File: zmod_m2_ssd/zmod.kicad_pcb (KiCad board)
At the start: 6 copper layers, 50 x 70 mm, 16 parts, among them J1 MDT420M02001, J2 QTH-020-01-X-D-DP-A, U1 SN74LVC1T45DBV

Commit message: adding clock chips for M.2
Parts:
- added U2: LTC6957xMS-2, Package_SO:MSOP-12_3x4mm_P0.65mm, F.Cu at (112.0, 89.0)
- added X1: ECS-2520MV-xxx-xx, Oscillator:Oscillator_SMD_ECS_2520MV-xxx-xx-4Pin_2.5x2.0mm, F.Cu at (105.0, 90.0)

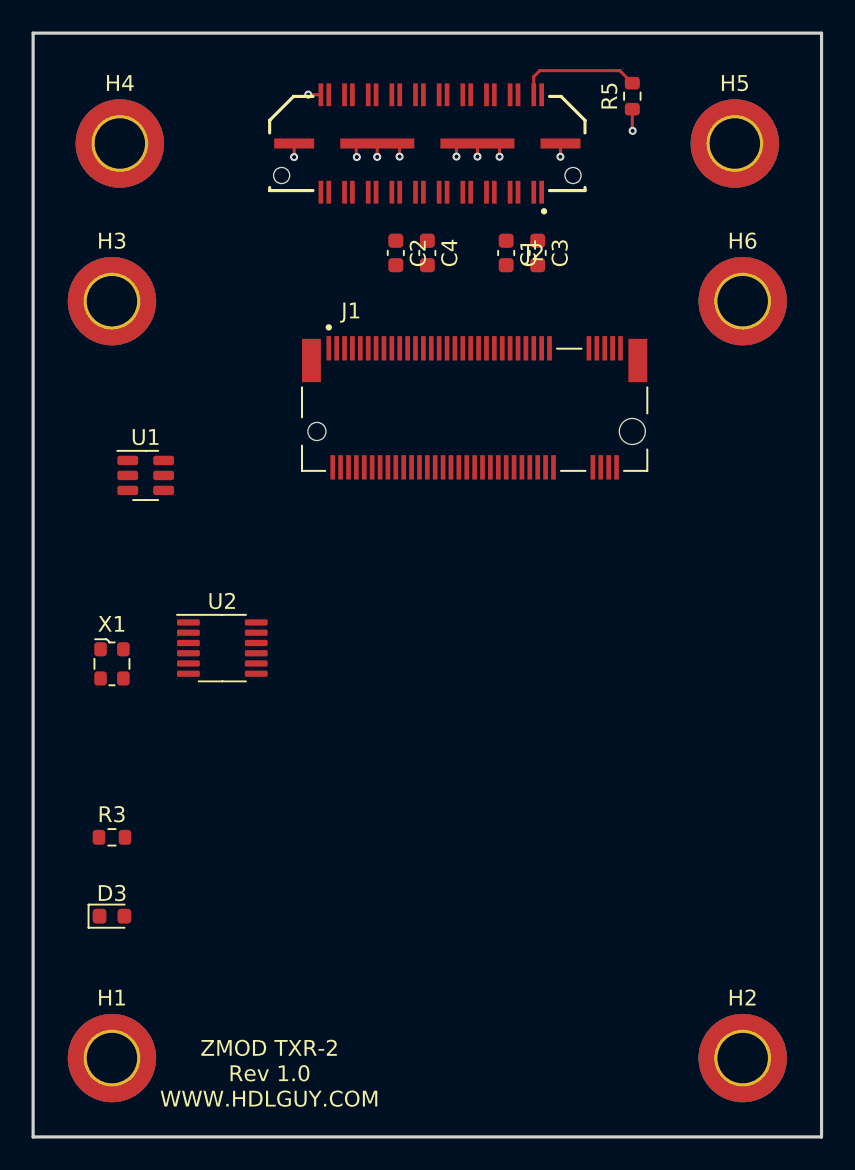
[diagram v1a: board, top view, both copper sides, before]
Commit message: placed all components and locked down mounting holes and connectors, need M.2 screw hole
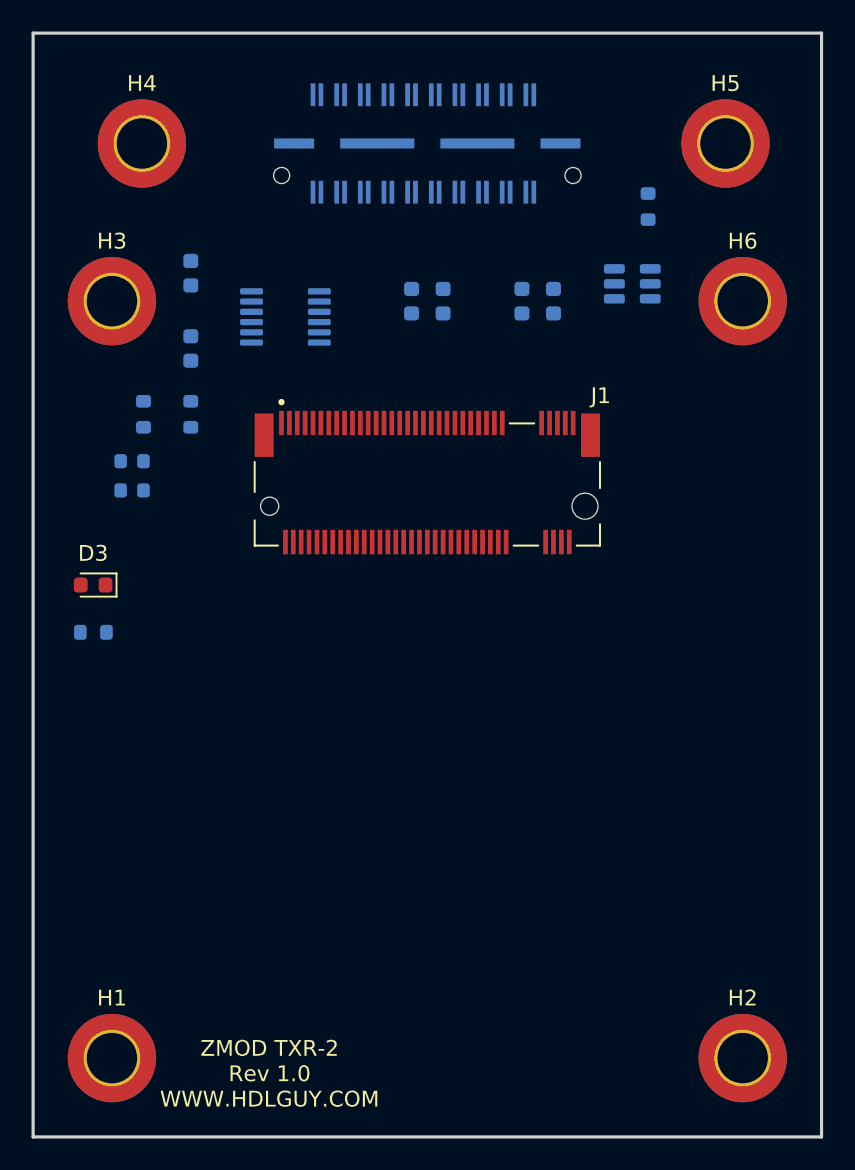
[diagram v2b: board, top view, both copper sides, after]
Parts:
- added C5: 0.01uf, Capacitor_SMD:C_0603_1608Metric, B.Cu at (110.0, 65.2)
- added C6: 0.01uf, Capacitor_SMD:C_0603_1608Metric, B.Cu at (110.0, 70.0)
- added R1: 100, Resistor_SMD:R_0603_1608Metric, B.Cu at (107.0, 74.2)
- added R2: 49.9, Resistor_SMD:R_0603_1608Metric, B.Cu at (110.0, 74.2)
- C1, C2, C3, C4: value C -> 0.01uf; moved to B.Cu
- J2, R3, R5, U1, U2: moved to B.Cu
- X1: value ECS-2520MV-xxx-xx -> ECS-2520MVQ-1000-BN-TR; moved to B.Cu
- moved U1 33.2 mm to (138.0, 65.9), turned to 180 degrees
- moved U2 21.4 mm to (116.0, 68.0)
- moved D3 21.0 mm to (103.8, 85.0), turned to 180 degrees
- moved R3 13.1 mm to (103.8, 88.0), turned to 180 degrees
- moved X1 12.0 mm to (106.3, 78.1)
- moved R5 7.07 mm to (139.0, 61.0)
- moved J1 5.61 mm to (125.0, 80.0)
- moved C1 3.22 mm to (131.0, 67.0)
- moved C2 3.22 mm to (124.0, 67.0)
- moved C3 3.22 mm to (133.0, 67.0)
- moved C4 3.22 mm to (126.0, 67.0)
- moved H4 1.40 mm to (106.9, 57.0)
- moved H5 0.59 mm to (143.9, 57.0)
- turned J2 to 0 degrees
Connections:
- net Net-(C1-Pad2) renamed /gtr0_txn_cc
- net Net-(C2-Pad2) renamed /gtr1_txn_cc
- net Net-(C3-Pad2) renamed /gtr0_txp_cc
- net Net-(C4-Pad2) renamed /gtr1_txp_cc
- J1 pad 53: unconnected-(J1-Pad53) -> Net-(U2-Pad11)
- J1 pad 55: unconnected-(J1-Pad55) -> Net-(U2-Pad10)
- U2 pad 1: unconnected-(U2-Pad1) -> GND
- U2 pad 10: unconnected-(U2-Pad10) -> Net-(U2-Pad10)
- U2 pad 11: unconnected-(U2-Pad11) -> Net-(U2-Pad11)
- U2 pad 12: unconnected-(U2-Pad12) -> GND
- U2 pad 2: unconnected-(U2-Pad2) -> +3V3
- U2 pad 3: unconnected-(U2-Pad3) -> Net-(C6-Pad2)
- U2 pad 4: unconnected-(U2-Pad4) -> Net-(C5-Pad2)
- U2 pad 5: unconnected-(U2-Pad5) -> GND
- U2 pad 6: unconnected-(U2-Pad6) -> +3V3
- U2 pad 7: unconnected-(U2-Pad7) -> GND
- U2 pad 8: unconnected-(U2-Pad8) -> /gtrclk0_p
- U2 pad 9: unconnected-(U2-Pad9) -> /gtrclk0_n
- X1 pad 2: unconnected-(X1-Pad2) -> GND
- X1 pad 3: unconnected-(X1-Pad3) -> Net-(R1-Pad2)
- X1 pad 4: unconnected-(X1-Pad4) -> +3V3
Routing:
- net /R_GA: track 7.89 -> 0.00 mm
- net GND: track 6.59 -> 0.00 mm, vias 8 -> 0
- net +3V3: track 2.19 -> 0.00 mm, vias 2 -> 0

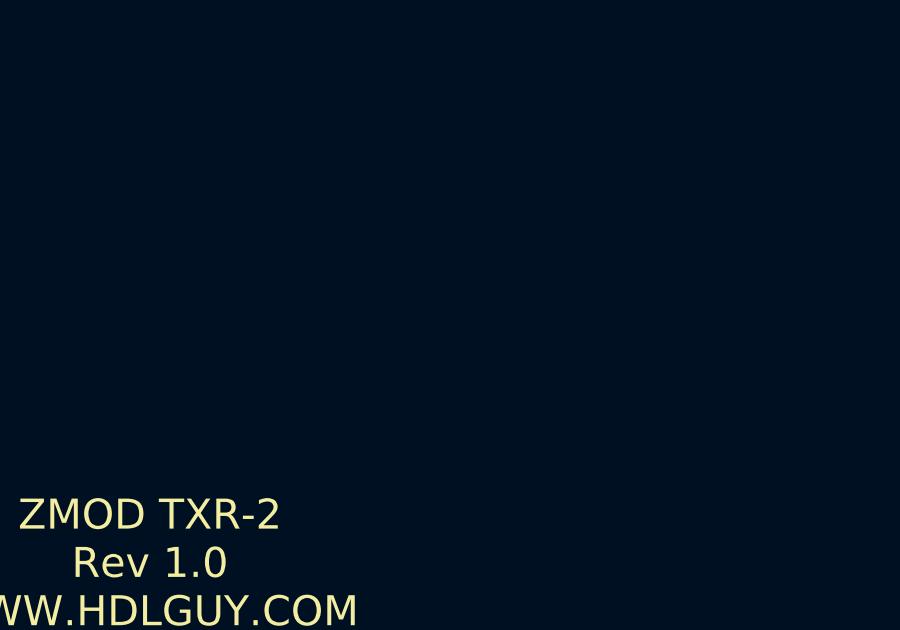
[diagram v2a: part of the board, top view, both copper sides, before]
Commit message: added mounting hole for M.2 screw
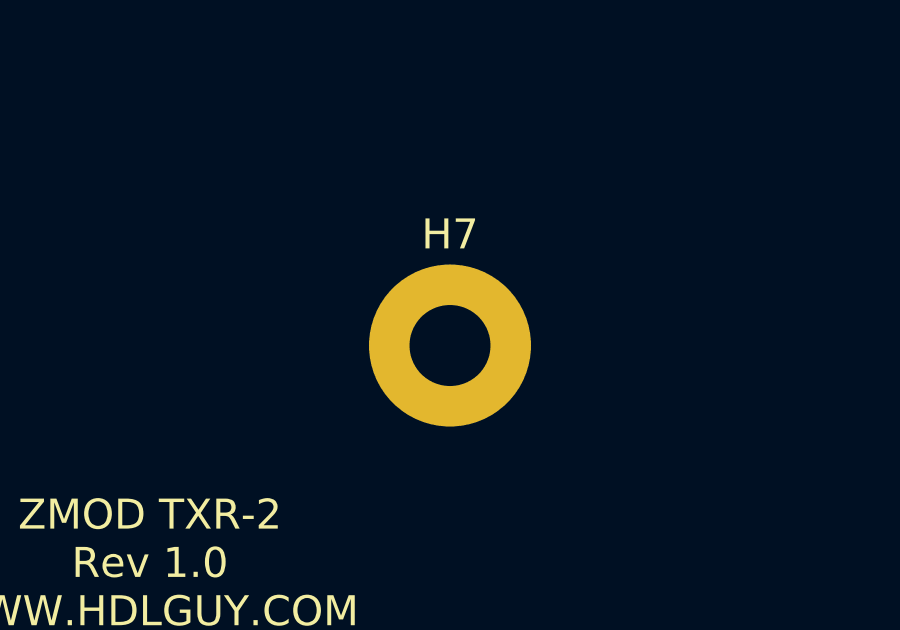
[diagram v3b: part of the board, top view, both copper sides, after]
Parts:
- added H7: MountingHole_Pad, MountingHole:MountingHole_2.7mm_Pad, F.Cu at (125.0, 108.8)
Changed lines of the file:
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@@
   (net 77 "+1V8")
   (net 78 "Net-(C6-Pad2)")
-  (net 79 "Net-(U2-Pad11)")
-  (net 80 "Net-(U2-Pad10)")
+  (net 79 "unconnected-(H7-Pad1)")
+  (net 80 "Net-(J1-Pad53)")
   (net 81 "Net-(R1-Pad2)")
   (net 82 "unconnected-(X1-Pad1)")
+  (net 83 "Net-(J1-Pad55)")
+  (footprint "MountingHole:MountingHole_2.7mm_Pad" locked (layer "F.Cu")
+    (at 125 108.75)
+    (descr "Mounting Hole 2.7mm")
+    (tags "mounting hole 2.7mm")
+    (property "Sheetfile" "zmod.kicad_sch")
+    (property "Sheetname" "")
+    (attr exclude_from_pos_files)
+    (fp_text reference "H7" (at 0 -3.7) (layer "F.SilkS")
+      (effects (font (size 1 1) (thickness 0.15)))
+    )
+    (fp_text value "MountingHole_Pad" (at 0 3.7) (layer "F.Fab")
+      (effects (font (size 1 1) (thickness 0.15)))
+    )
+    (fp_text user "${REFERENCE}" (at 0 0) (layer "F.Fab")
+      (effects (font (size 1 1) (thickness 0.15)))
+    )
+    (fp_circle (center 0 0) (end 2.7 0) (layer "Cmts.User") (width 0.15) (fill none))
+    (fp_circle (center 0 0) (end 2.95 0) (layer "F.CrtYd") (width 0.05) (fill none))
+    (pad "1" thru_hole circle locked (at 0 0) (size 5.4 5.4) (drill 2.7) (layers *.Cu *.Mask)
+      (net 79 "unconnected-(H7-Pad1)") (pinfunction "1") (pintype "input"))
+  )
   (footprint "MountingHole:MountingHole_3.2mm_M3_DIN965_Pad_TopBottom" locked (layer "F.Cu")
     (at 145 67)
@@
       (net 66 "unconnected-(J1-Pad52)") (pinfunction "~{CLKREQ}") (pintype "bidirectional+no_connect"))
     (pad "53" smd rect locked (at 3.75 -5.275) (size 0.3 1.55) (layers "F.Cu" "F.Paste" "F.Mask")
-      (net 79 "Net-(U2-Pad11)") (pinfunction "REFCLKn") (pintype "output"))
+      (net 80 "Net-(J1-Pad53)") (pinfunction "REFCLKn") (pintype "output"))
     (pad "54" smd rect locked (at 4 2.275) (size 0.3 1.55) (layers "F.Cu" "F.Paste" "F.Mask")
       (net 67 "unconnected-(J1-Pad54)") (pinfunction "~{PEWAKE}") (pintype "bidirectional+no_connect"))
     (pad "55" smd rect locked (at 4.25 -5.275) (size 0.3 1.55) (layers "F.Cu" "F.Paste" "F.Mask")
-      (net 80 "Net-(U2-Pad10)") (pinfunction "REFCLKp") (pintype "output"))
+      (net 83 "Net-(J1-Pad55)") (pinfunction "REFCLKp") (pintype "output"))
     (pad "56" smd rect locked (at 4.5 2.275) (size 0.3 1.55) (layers "F.Cu" "F.Paste" "F.Mask")
       (net 68 "unconnected-(J1-Pad56)") (pinfunction "NC") (pintype "no_connect"))
@@
       (net 74 "/gtrclk0_n") (pinfunction "OUT2-") (pintype "output"))
     (pad "10" smd roundrect (at 2.15 0.325) (size 1.45 0.4) (layers "B.Cu" "B.Paste" "B.Mask") (roundrect_rratio 0.25)
-      (net 80 "Net-(U2-Pad10)") (pinfunction "OUT1-") (pintype "output"))
+      (net 83 "Net-(J1-Pad55)") (pinfunction "OUT1-") (pintype "output"))
     (pad "11" smd roundrect (at 2.15 0.975) (size 1.45 0.4) (layers "B.Cu" "B.Paste" "B.Mask") (roundrect_rratio 0.25)
-      (net 79 "Net-(U2-Pad11)") (pinfunction "OUT1+") (pintype "output"))
+      (net 80 "Net-(J1-Pad53)") (pinfunction "OUT1+") (pintype "output"))
     (pad "12" smd roundrect (at 2.15 1.625) (size 1.45 0.4) (layers "B.Cu" "B.Paste" "B.Mask") (roundrect_rratio 0.25)
       (net 1 "GND") (pinfunction "SD1") (pintype "input"))
